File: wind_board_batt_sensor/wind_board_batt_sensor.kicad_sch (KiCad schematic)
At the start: 31 parts, among them J1 Batt +, J2 Batt -, J3 Sys +, J4 Sys -, U1 MAX17263xxTE, U2 PTSM82903SISB2R, U3 ATtiny402-SS

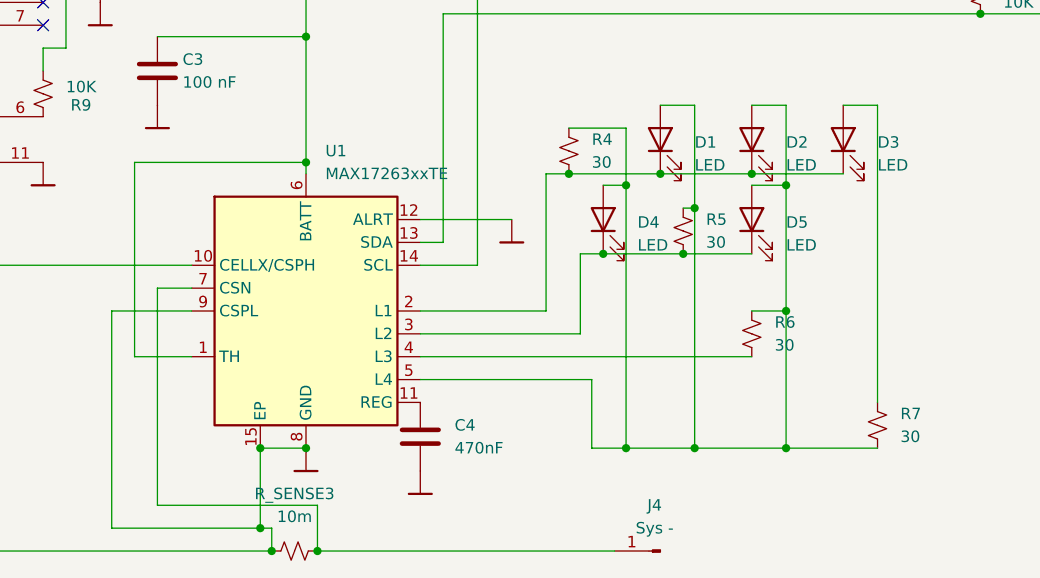
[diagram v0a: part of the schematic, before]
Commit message: All components to 0805 on battery board
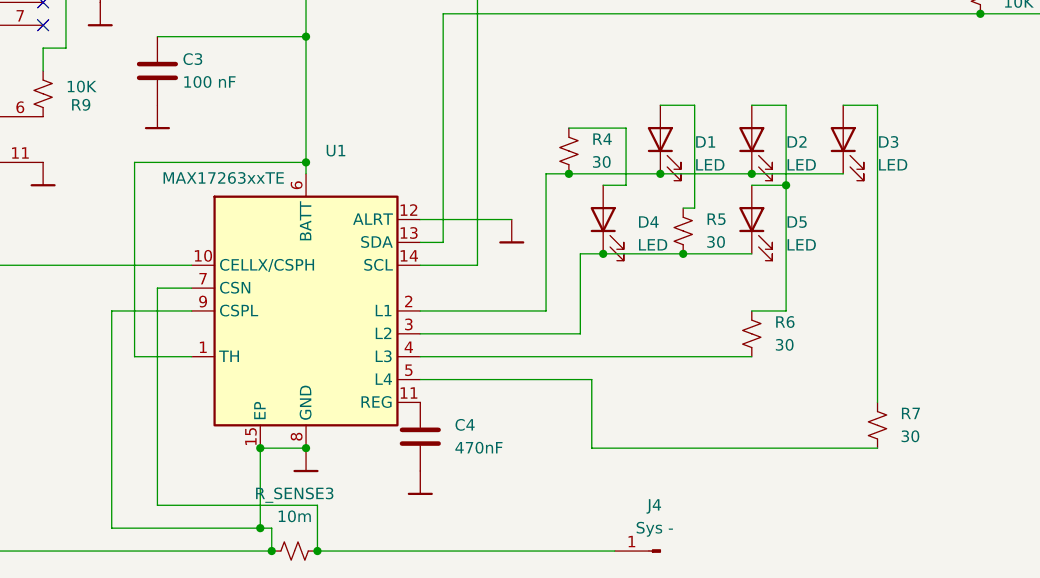
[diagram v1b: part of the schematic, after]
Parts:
- C1, C3, C4: footprint Capacitor_SMD:C_0402_1005Metric -> Resistor_SMD:R_0805_2012Metric_Pad1.20x1.40mm_HandSolder
- C2, C5, C6: footprint Capacitor_SMD:C_0805_2012Metric -> Resistor_SMD:R_0805_2012Metric_Pad1.20x1.40mm_HandSolder
- R1, R10, R11, R2, R8: footprint Resistor_SMD:R_0805_2012Metric -> Resistor_SMD:R_0805_2012Metric_Pad1.20x1.40mm_HandSolder
- R3, R4, R5, R6, R7, R9: footprint Resistor_SMD:R_0402_1005Metric -> Resistor_SMD:R_0805_2012Metric_Pad1.20x1.40mm_HandSolder
- R_SENSE3: footprint Resistor_SMD:R_1206_3216Metric -> Resistor_SMD:R_1206_3216Metric_Pad1.30x1.75mm_HandSolder
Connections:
- new net: D2.2 (A), D5.2 (A), R6.1
- new net: D4.2 (A), R4.1
- new net: R7.2, U1.5 (L4)
- new net: D1.2 (A), R5.1
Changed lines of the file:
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@@
 	(paper "A4")
 	(junction
-		(at 172.72 74.93)
-		(diameter 0)
-		(color 0 0 0 0)
-	)
-	(junction
 		(at 187.96 50.8)
 		(diameter 0)
@@
 	)
 	(junction
-		(at 172.72 101.6)
-		(diameter 0)
-		(color 0 0 0 0)
-	)
-	(junction
 		(at 64.77 46.99)
 		(diameter 0)
@@
 	)
 	(junction
-		(at 182.88 86.36)
-		(diameter 0)
-		(color 0 0 0 0)
-	)
-	(junction
 		(at 158.75 71.12)
 		(diameter 0)
@@
 	)
 	(junction
-		(at 165.1 101.6)
-		(diameter 0)
-		(color 0 0 0 0)
-	)
-	(junction
 		(at 129.54 101.6)
 		(diameter 0)
@@
 	)
 	(junction
-		(at 165.1 72.39)
-		(diameter 0)
-		(color 0 0 0 0)
-	)
-	(junction
 		(at 238.76 35.56)
 		(diameter 0)
@@
 		(color 0 0 0 0)
 	)
-	(junction
-		(at 182.88 101.6)
-		(diameter 0)
-		(color 0 0 0 0)
-	)
 	(no_connect
 		(at 100.33 52.07)
@@
 	(wire
 		(pts
-			(xy 182.88 86.36) (xy 182.88 101.6)
-		)
-		(stroke
-			(width 0)
-			(type default)
-		)
-	)
-	(wire
-		(pts
 			(xy 102.87 57.15) (xy 102.87 46.99)
 		)
@@
 	(wire
 		(pts
-			(xy 172.72 74.93) (xy 172.72 101.6)
-		)
-		(stroke
-			(width 0)
-			(type default)
-		)
-	)
-	(wire
-		(pts
 			(xy 53.34 71.12) (xy 53.34 73.66)
 		)
@@
 	(wire
 		(pts
-			(xy 161.29 101.6) (xy 165.1 101.6)
-		)
-		(stroke
-			(width 0)
-			(type default)
-		)
-	)
-	(wire
-		(pts
 			(xy 142.24 86.36) (xy 156.21 86.36)
 		)
@@
 	(wire
 		(pts
-			(xy 182.88 101.6) (xy 193.04 101.6)
-		)
-		(stroke
-			(width 0)
-			(type default)
-		)
-	)
-	(wire
-		(pts
 			(xy 130.81 107.95) (xy 130.81 113.03)
 		)
@@
 	(wire
 		(pts
-			(xy 172.72 101.6) (xy 182.88 101.6)
+			(xy 161.29 101.6) (xy 193.04 101.6)
 		)
 		(stroke
@@
 	(wire
 		(pts
-			(xy 165.1 72.39) (xy 165.1 101.6)
-		)
-		(stroke
-			(width 0)
-			(type default)
-		)
-	)
-	(wire
-		(pts
 			(xy 129.54 55.88) (xy 129.54 69.85)
 		)
@@
 	(wire
 		(pts
-			(xy 165.1 101.6) (xy 172.72 101.6)
-		)
-		(stroke
-			(width 0)
-			(type default)
-		)
-	)
-	(wire
-		(pts
 			(xy 162.56 72.39) (xy 165.1 72.39)
 		)
@@
 			)
 		)
-		(property "Footprint" "Resistor_SMD:R_0402_1005Metric"
+		(property "Footprint" "Resistor_SMD:R_0805_2012Metric_Pad1.20x1.40mm_HandSolder"
 			(at 26.67 77.47 0)
 			(effects
@@
 			)
 		)
-		(property "Footprint" "Resistor_SMD:R_1206_3216Metric"
+		(property "Footprint" "Resistor_SMD:R_1206_3216Metric_Pad1.30x1.75mm_HandSolder"
 			(at 128.27 113.03 0)
 			(effects
@@
 			)
 		)
-		(property "Footprint" "Capacitor_SMD:C_0805_2012Metric"
+		(property "Footprint" "Resistor_SMD:R_0805_2012Metric_Pad1.20x1.40mm_HandSolder"
 			(at 246.38 34.5948 0)
 			(effects
@@
 		(on_board yes)
 		(dnp no)
-		(fields_autoplaced yes)
 		(property "Reference" "U1"
 			(at 131.6833 68.58 0)
@@
 		)
 		(property "Value" "MAX17263xxTE"
-			(at 131.6833 71.12 0)
+			(at 113.538 71.628 0)
 			(effects
 				(font
@@
 			)
 		)
-		(property "Footprint" "Resistor_SMD:R_0805_2012Metric"
+		(property "Footprint" "Resistor_SMD:R_0805_2012Metric_Pad1.20x1.40mm_HandSolder"
 			(at 53.34 76.2 0)
 			(effects
@@
 			)
 		)
-		(property "Footprint" "Resistor_SMD:R_0805_2012Metric"
+		(property "Footprint" "Resistor_SMD:R_0805_2012Metric_Pad1.20x1.40mm_HandSolder"
 			(at 53.34 68.58 0)
 			(effects
@@
 			)
 		)
-		(property "Footprint" "Capacitor_SMD:C_0805_2012Metric"
+		(property "Footprint" "Resistor_SMD:R_0805_2012Metric_Pad1.20x1.40mm_HandSolder"
 			(at 238.76 38.4048 0)
 			(effects
@@
 			)
 		)
-		(property "Footprint" "Resistor_SMD:R_0805_2012Metric"
+		(property "Footprint" "Resistor_SMD:R_0805_2012Metric_Pad1.20x1.40mm_HandSolder"
 			(at 187.96 48.26 0)
 			(effects
@@
 			)
 		)
-		(property "Footprint" "Capacitor_SMD:C_0402_1005Metric"
+		(property "Footprint" "Resistor_SMD:R_0805_2012Metric_Pad1.20x1.40mm_HandSolder"
 			(at 143.2052 104.14 0)
 			(effects
@@
 			)
 		)
-		(property "Footprint" "Capacitor_SMD:C_0805_2012Metric"
+		(property "Footprint" "Resistor_SMD:R_0805_2012Metric_Pad1.20x1.40mm_HandSolder"
 			(at 107.6452 52.07 0)
 			(effects
@@
 			)
 		)
-		(property "Footprint" "Capacitor_SMD:C_0402_1005Metric"
+		(property "Footprint" "Resistor_SMD:R_0805_2012Metric_Pad1.20x1.40mm_HandSolder"
 			(at 56.8452 54.61 0)
 			(effects
@@
 			)
 		)
-		(property "Footprint" "Resistor_SMD:R_0402_1005Metric"
+		(property "Footprint" "Resistor_SMD:R_0805_2012Metric_Pad1.20x1.40mm_HandSolder"
 			(at 100.33 62.23 0)
 			(effects
@@
 			)
 		)
-		(property "Footprint" "Resistor_SMD:R_0805_2012Metric"
+		(property "Footprint" "Resistor_SMD:R_0805_2012Metric_Pad1.20x1.40mm_HandSolder"
 			(at 53.34 83.82 0)
 			(effects
@@
 			)
 		)
-		(property "Footprint" "Resistor_SMD:R_0402_1005Metric"
+		(property "Footprint" "Resistor_SMD:R_0805_2012Metric_Pad1.20x1.40mm_HandSolder"
 			(at 158.75 68.58 0)
 			(effects
@@
 			)
 		)
-		(property "Footprint" "Capacitor_SMD:C_0402_1005Metric"
+		(property "Footprint" "Resistor_SMD:R_0805_2012Metric_Pad1.20x1.40mm_HandSolder"
 			(at 113.9952 63.5 0)
 			(effects
@@
 			)
 		)
-		(property "Footprint" "Resistor_SMD:R_0402_1005Metric"
+		(property "Footprint" "Resistor_SMD:R_0805_2012Metric_Pad1.20x1.40mm_HandSolder"
 			(at 171.45 77.47 0)
 			(effects
@@
 			)
 		)
-		(property "Footprint" "Resistor_SMD:R_0402_1005Metric"
+		(property "Footprint" "Resistor_SMD:R_0805_2012Metric_Pad1.20x1.40mm_HandSolder"
 			(at 179.07 88.9 0)
 			(effects
@@
 			)
 		)
-		(property "Footprint" "Resistor_SMD:R_0805_2012Metric"
+		(property "Footprint" "Resistor_SMD:R_0805_2012Metric_Pad1.20x1.40mm_HandSolder"
 			(at 204.47 50.8 0)
 			(effects
@@
 			)
 		)
-		(property "Footprint" "Resistor_SMD:R_0402_1005Metric"
+		(property "Footprint" "Resistor_SMD:R_0805_2012Metric_Pad1.20x1.40mm_HandSolder"
 			(at 193.04 99.06 0)
 			(effects

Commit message: swap sda-scl pins
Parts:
- removed J_PA0: TestPoint, TestPoint:TestPoint_Pad_4.0x4.0mm, symbol Connector:TestPoint
- added J5: Conn_01x03_Socket, Connector_PinHeader_2.54mm:PinHeader_1x03_P2.54mm_Vertical, symbol Connector:Conn_01x03_Socket
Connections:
- net +3.3V: now also J5.1 (Pin_1)
- net at U3.6 (~{RESET}/PA0): now also J5.2 (Pin_2)
- net at R11.2, U1.13 (SDA): now also U3.4 (PA1); no longer U3.5 (PA2)
- net at R10.2, U1.14 (SCL): now also U3.5 (PA2); no longer U3.4 (PA1)
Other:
- moved on the sheet: R10, R11

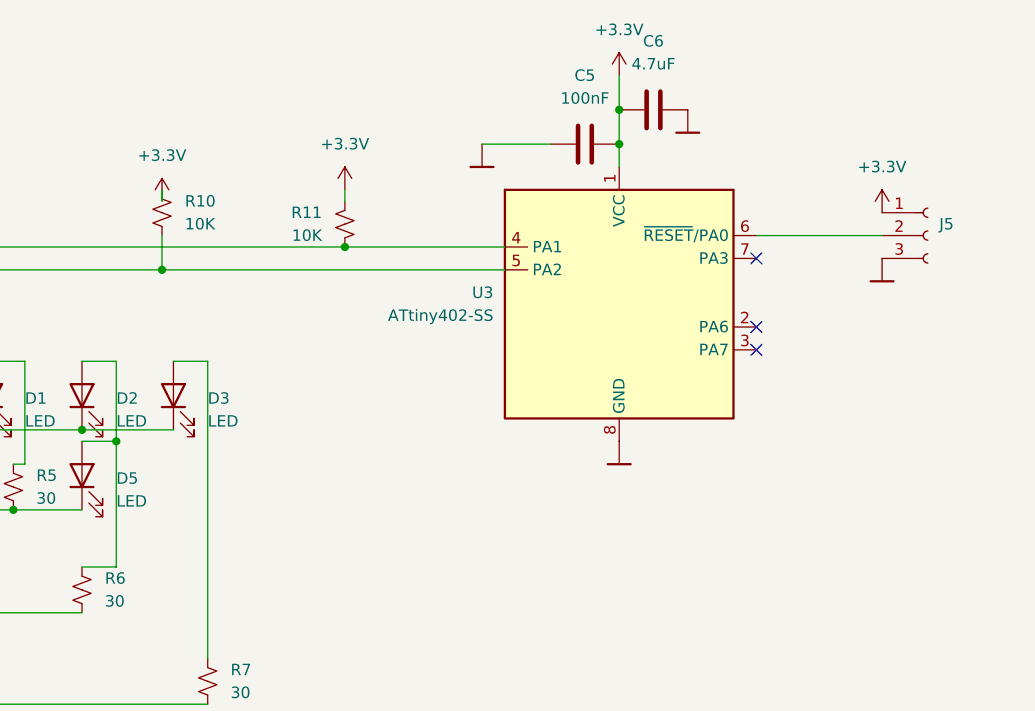
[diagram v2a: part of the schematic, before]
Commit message: add led and sca-scl header
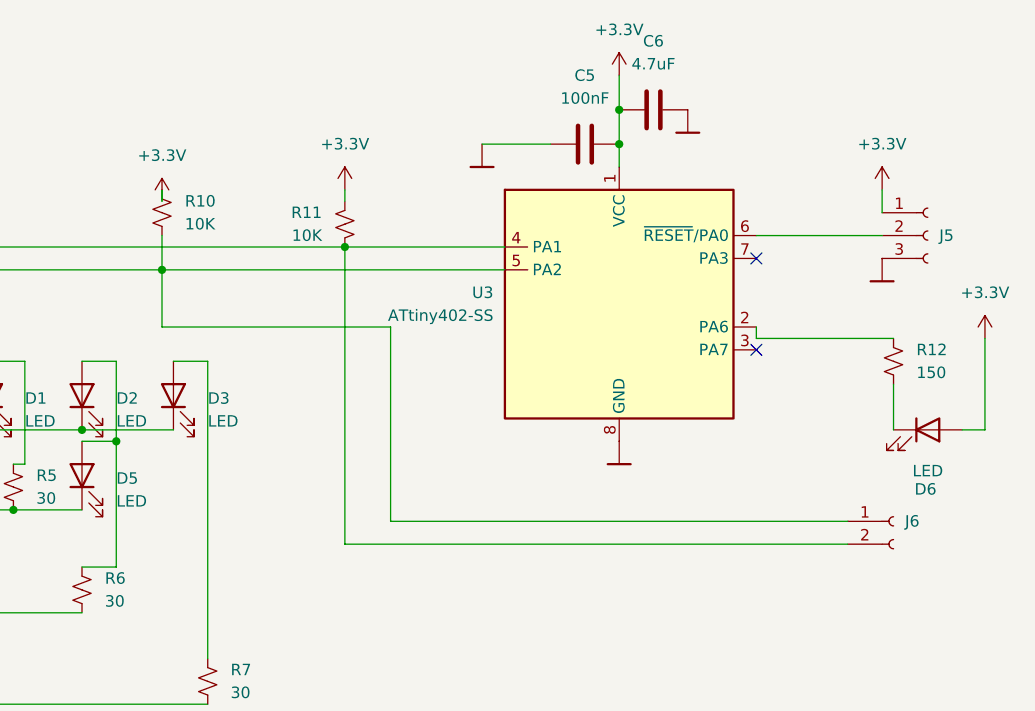
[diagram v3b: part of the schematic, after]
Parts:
- added D6: LED, LED_SMD:LED_0805_2012Metric, symbol Device:LED
- added J6: Conn_01x02_Socket, Connector_PinHeader_2.54mm:PinHeader_1x02_P2.54mm_Vertical, symbol Connector:Conn_01x02_Socket
- added R12: 150, Resistor_SMD:R_0805_2012Metric, symbol Device:R_Small_US
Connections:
- net +3.3V: now also D6.2 (A)
- net at R11.2, U1.13 (SDA), U3.4 (PA1): now also J6.2 (Pin_2)
- net at R10.2, U1.14 (SCL), U3.5 (PA2): now also J6.1 (Pin_1)
- net at U3.2 (PA6): now also R12.2
- new net: D6.1 (K), R12.1
- no-connect marks 6 -> 5

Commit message: fix stuff
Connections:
- net at U3.6 (~{RESET}/PA0): now also J5.3 (Pin_3); no longer J5.2 (Pin_2)
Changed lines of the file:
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@@
 	(wire
 		(pts
+			(xy 269.24 38.1) (xy 267.97 38.1)
+		)
+		(stroke
+			(width 0)
+			(type default)
+		)
+	)
+	(wire
+		(pts
 			(xy 53.34 44.45) (xy 53.34 66.04)
 		)
@@
 	(wire
 		(pts
+			(xy 267.97 38.1) (xy 267.97 46.99)
+		)
+		(stroke
+			(width 0)
+			(type default)
+		)
+	)
+	(wire
+		(pts
 			(xy 182.88 63.5) (xy 182.88 72.39)
 		)
@@
 	(wire
 		(pts
+			(xy 267.97 49.53) (xy 264.16 49.53)
+		)
+		(stroke
+			(width 0)
+			(type default)
+		)
+	)
+	(wire
+		(pts
 			(xy 193.04 63.5) (xy 193.04 96.52)
 		)
@@
 	(wire
 		(pts
+			(xy 261.62 52.07) (xy 267.97 52.07)
+		)
+		(stroke
+			(width 0)
+			(type default)
+		)
+	)
+	(wire
+		(pts
 			(xy 107.95 110.49) (xy 124.46 110.49)
 		)
@@
 	(wire
 		(pts
-			(xy 267.97 44.45) (xy 267.97 46.99)
+			(xy 269.24 35.56) (xy 269.24 38.1)
 		)
 		(stroke
@@
 	(wire
 		(pts
-			(xy 254 49.53) (xy 267.97 49.53)
-		)
-		(stroke
-			(width 0)
-			(type default)
-		)
-	)
-	(wire
-		(pts
 			(xy 238.76 35.56) (xy 238.76 39.37)
 		)
@@
 	(wire
 		(pts
+			(xy 264.16 49.53) (xy 264.16 52.07)
+		)
+		(stroke
+			(width 0)
+			(type default)
+		)
+	)
+	(wire
+		(pts
+			(xy 254 49.53) (xy 261.62 49.53)
+		)
+		(stroke
+			(width 0)
+			(type default)
+		)
+	)
+	(wire
+		(pts
 			(xy 179.07 71.12) (xy 189.23 71.12)
 		)
@@
 		)
 	)
+	(wire
+		(pts
+			(xy 261.62 52.07) (xy 261.62 49.53)
+		)
+		(stroke
+			(width 0)
+			(type default)
+		)
+	)
 	(symbol
 		(lib_id "power:GND")
@@
 	(symbol
 		(lib_id "power:GND")
-		(at 267.97 54.61 0)
+		(at 264.16 54.61 0)
 		(unit 1)
 		(exclude_from_sim no)
@@
 		(fields_autoplaced yes)
 		(property "Reference" "#0111"
-			(at 267.97 54.61 0)
+			(at 264.16 54.61 0)
 			(effects
 				(font
@@
 		)
 		(property "Value" "~"
-			(at 267.97 57.15 0)
+			(at 264.16 57.15 0)
 			(effects
 				(font
@@
 		)
 		(property "Footprint" ""
-			(at 267.97 54.61 0)
+			(at 264.16 54.61 0)
 			(effects
 				(font
@@
 		)
 		(property "Datasheet" ""
-			(at 267.97 54.61 0)
+			(at 264.16 54.61 0)
 			(effects
 				(font
@@
 		)
 		(property "Description" "GND"
-			(at 267.97 54.61 0)
+			(at 264.16 54.61 0)
 			(effects
 				(font
@@
 	(symbol
 		(lib_id "power:+3.3V")
-		(at 267.97 44.45 0)
+		(at 269.24 35.56 0)
 		(unit 1)
 		(exclude_from_sim no)
@@
 		(fields_autoplaced yes)
 		(property "Reference" "#PWR05"
-			(at 267.97 48.26 0)
+			(at 269.24 39.37 0)
 			(effects
 				(font
@@
 		)
 		(property "Value" "+3.3V"
-			(at 267.97 39.37 0)
+			(at 269.24 30.48 0)
 			(effects
 				(font
@@
 		)
 		(property "Footprint" ""
-			(at 267.97 44.45 0)
+			(at 269.24 35.56 0)
 			(effects
 				(font
@@
 		)
 		(property "Datasheet" ""
-			(at 267.97 44.45 0)
+			(at 269.24 35.56 0)
 			(effects
 				(font
@@
 		)
 		(property "Description" "Power symbol creates a global label with name \"+3.3V\""
-			(at 267.97 44.45 0)
+			(at 269.24 35.56 0)
 			(effects
 				(font

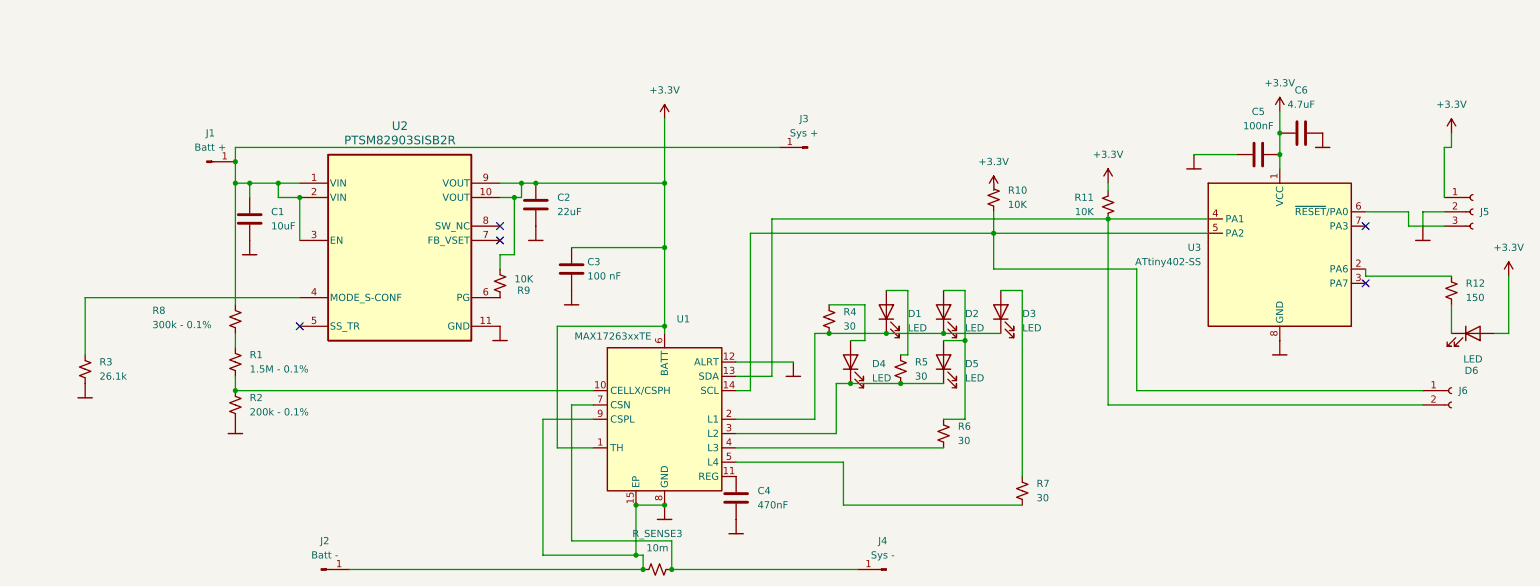
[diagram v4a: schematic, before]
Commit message: new power supply
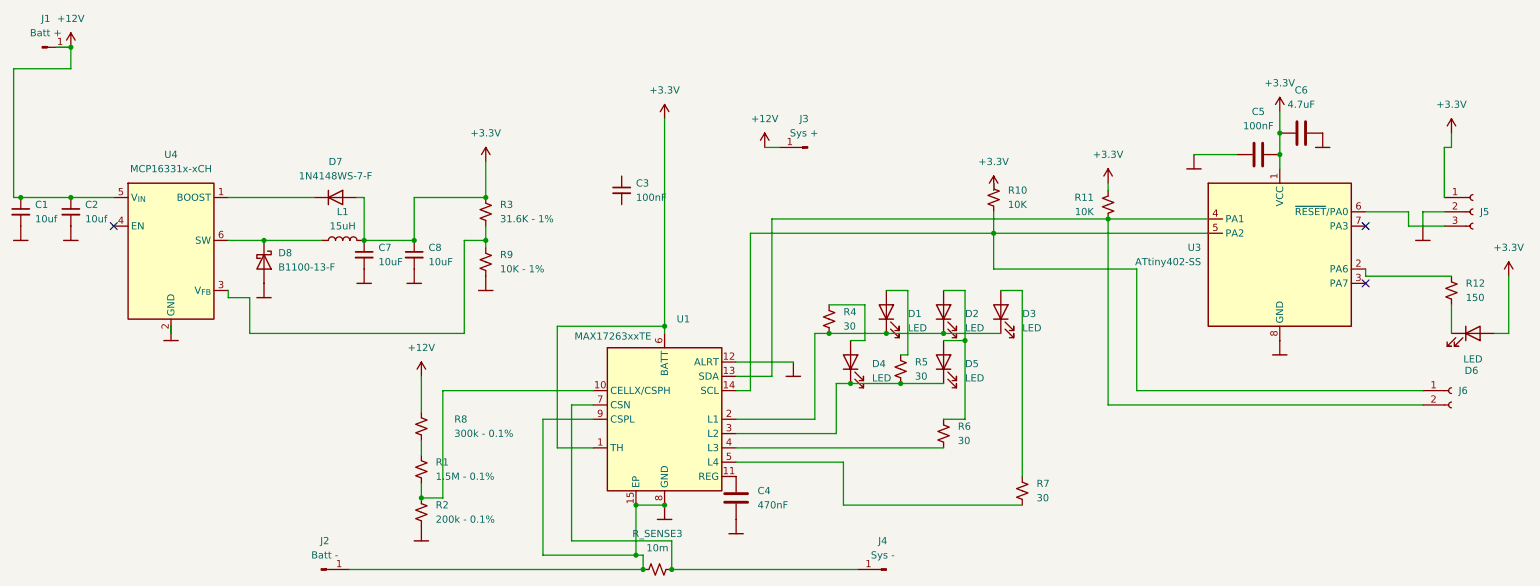
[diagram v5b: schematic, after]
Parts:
- removed C1: 10uF, Resistor_SMD:R_0805_2012Metric_Pad1.20x1.40mm_HandSolder, symbol Device:C
- removed C2: 22uF, Resistor_SMD:R_0805_2012Metric_Pad1.20x1.40mm_HandSolder, symbol Device:C
- removed C3: 100 nF, Resistor_SMD:R_0805_2012Metric_Pad1.20x1.40mm_HandSolder, symbol Device:C
- removed U2: PTSM82903SISB2R, TPSM82903:SIS0011A-MFG, symbol PTSM82903SISB2R:PTSM82903SISB2R
- added C1, C2: 10uf, Capacitor_SMD:C_1210_3225Metric, symbol Device:C_Small
- added C3: 100nF, Capacitor_SMD:C_0603_1608Metric, symbol Device:C_Small
- added C7, C8: 10uF, Capacitor_SMD:C_0805_2012Metric, symbol Device:C_Small
- added D7: 1N4148WS-7-F, Diode_SMD:D_SOD-323, symbol Device:D
- added D8: B1100-13-F, Diode_SMD:D_SMA, symbol Device:D_Schottky
- added L1: 15uH, Inductor_SMD:L_7.3x7.3_H4.5, symbol Device:L
- added U4: MCP16331x-xCH, Package_TO_SOT_SMD:SOT-23-6, symbol Regulator_Switching:MCP16331x-xCH
- R3: value 26.1k -> 31.6K - 1%; footprint Resistor_SMD:R_0805_2012Metric_Pad1.20x1.40mm_HandSolder -> Resistor_SMD:R_0805_2012Metric
- R9: value 10K -> 10K - 1%; footprint Resistor_SMD:R_0805_2012Metric_Pad1.20x1.40mm_HandSolder -> Resistor_SMD:R_0805_2012Metric
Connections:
- net +3.3V: now also R3.1, C7.1, C8.1, D7.2 (A), L1.2; no longer R9.1
- net at R3.2: now also R9.1, U4.3 (V_{FB})
- net +12V: now reaches J1.1 (Pin_1), J3.1 (Pin_1), R8.1
- net +12V: now also C1.1, C2.1, U4.5 (V_{IN})
- new net: D8.1 (K), L1.1, U4.6 (SW)
- new net: D7.1 (K), U4.1 (BOOST)
- no-connect marks 5 -> 3
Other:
- moved on the sheet: J1, R1, R2, R8
